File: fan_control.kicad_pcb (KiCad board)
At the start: 2 copper layers, 50 x 68.6 mm, 46 parts, among them J1 Conn_01x02_Male, J2 Conn_01x02_Male, J3 Conn_01x02_Male, J4 Conn_01x02_Male, J5 Conn_01x02_Male, J6 Conn_01x02_Male, J7 Conn_01x02_Male, J8 Conn_01x02_Male, Q10 BC557, Q11 BC557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

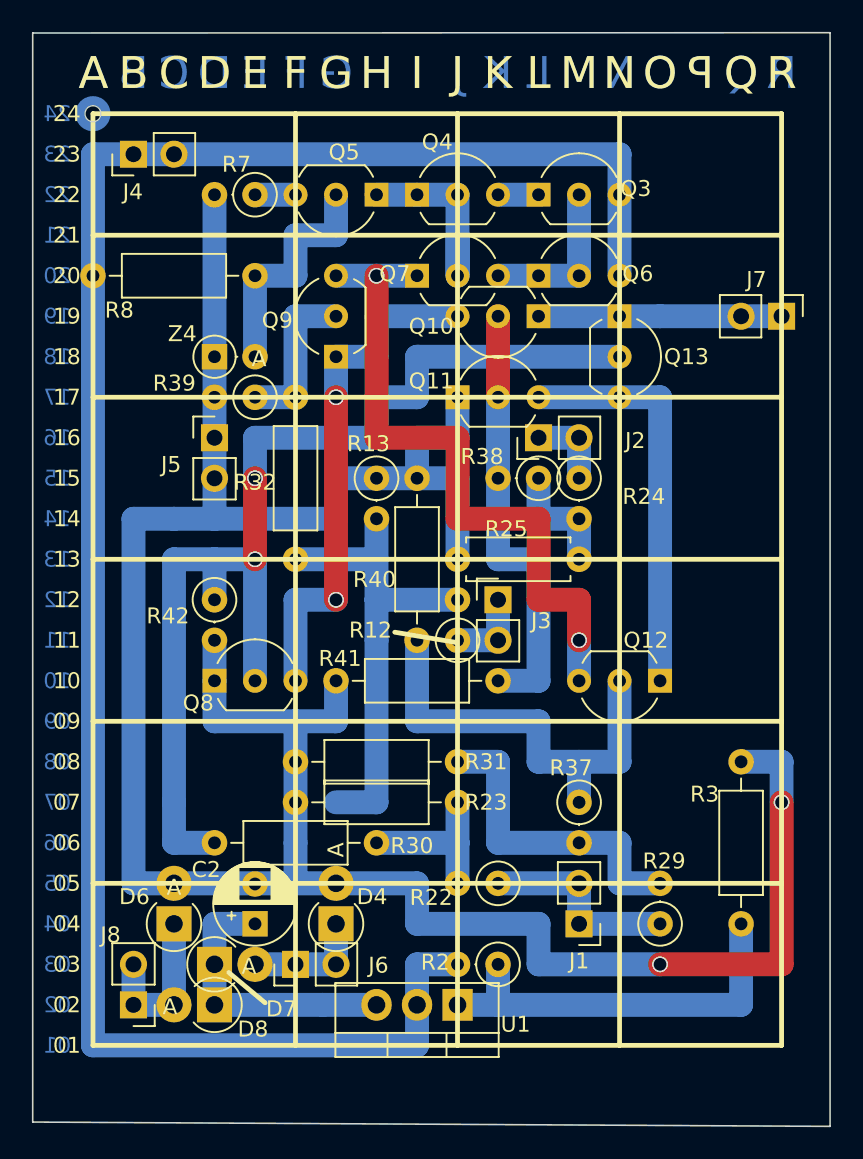
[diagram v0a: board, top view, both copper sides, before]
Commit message: add resistors to pcb
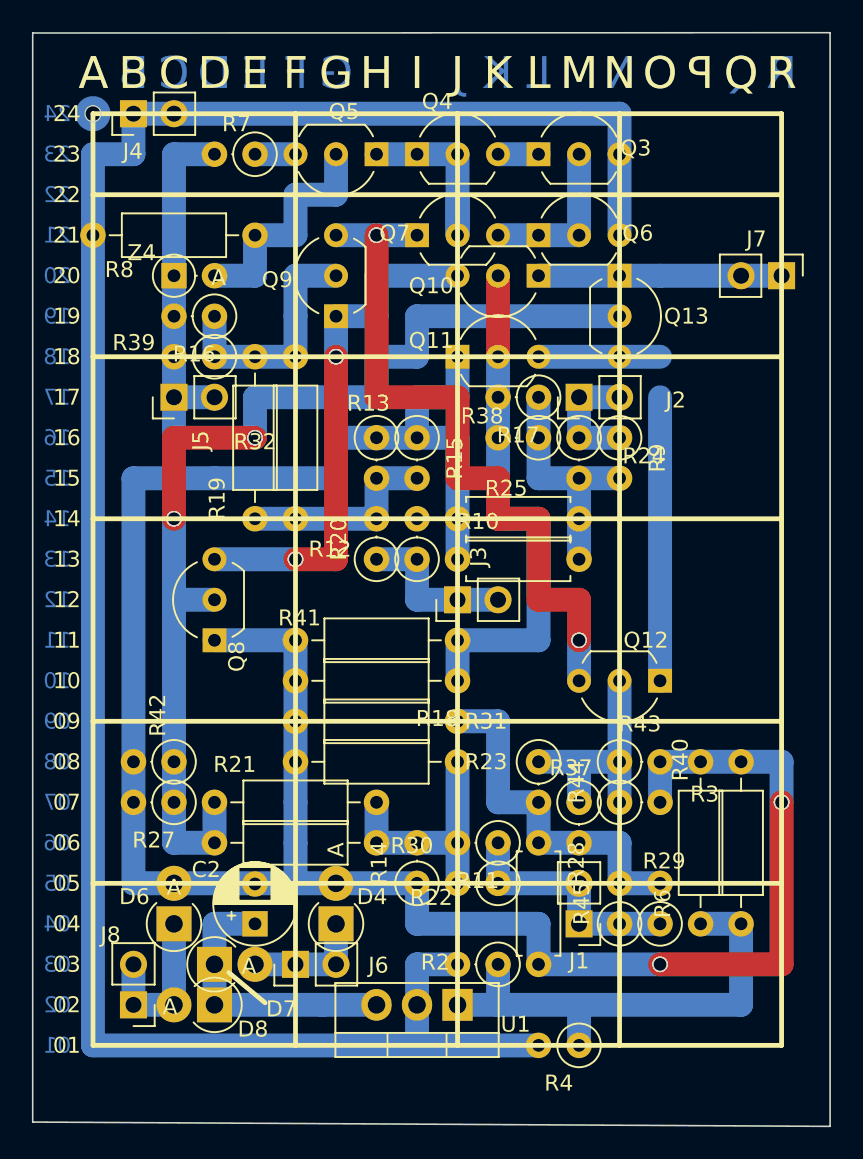
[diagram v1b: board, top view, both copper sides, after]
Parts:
- added R10: 100K, Resistor_THT:R_Axial_DIN0207_L6.3mm_D2.5mm_P7.62mm_Horizontal, F.Cu at (67.2, 63.5)
- added R11: 150K, Resistor_THT:R_Axial_DIN0207_L6.3mm_D2.5mm_P2.54mm_Vertical, F.Cu at (69.7, 81.3)
- added R14: 50K, Resistor_THT:R_Axial_DIN0207_L6.3mm_D2.5mm_P2.54mm_Vertical, F.Cu at (64.7, 83.9)
- added R15: 50k, Resistor_THT:R_Axial_DIN0207_L6.3mm_D2.5mm_P2.54mm_Vertical, F.Cu at (64.7, 55.9)
- added R16: 100K, Resistor_THT:R_Axial_DIN0207_L6.3mm_D2.5mm_P2.54mm_Vertical, F.Cu at (52.0, 48.3)
- added R17: 100K, Resistor_THT:R_Axial_DIN0207_L6.3mm_D2.5mm_P2.54mm_Vertical, F.Cu at (72.3, 53.4)
- added R18: 100K, Resistor_THT:R_Axial_DIN0207_L6.3mm_D2.5mm_P10.16mm_Horizontal, F.Cu at (67.2, 71.2)
- added R19: 100K, Resistor_THT:R_Axial_DIN0207_L6.3mm_D2.5mm_P10.16mm_Horizontal, F.Cu at (54.5, 61.0)
- added R20: 150k, Resistor_THT:R_Axial_DIN0207_L6.3mm_D2.5mm_P2.54mm_Vertical, F.Cu at (62.1, 63.5)
- added R21: 100K, Resistor_THT:R_Axial_DIN0207_L6.3mm_D2.5mm_P10.16mm_Horizontal, F.Cu at (52.0, 78.8)
- added R27: 100K, Resistor_THT:R_Axial_DIN0207_L6.3mm_D2.5mm_P2.54mm_Vertical, F.Cu at (49.4, 78.8)
- added R28: 50K, Resistor_THT:R_Axial_DIN0207_L6.3mm_D2.5mm_P7.62mm_Horizontal, F.Cu at (72.3, 81.3)
- added R4: R, Resistor_THT:R_Axial_DIN0207_L6.3mm_D2.5mm_P2.54mm_Vertical, F.Cu at (74.8, 94.0)
- added R43: 100K, Resistor_THT:R_Axial_DIN0207_L6.3mm_D2.5mm_P2.54mm_Vertical, F.Cu at (77.4, 76.2)
- added R44: 100K, Resistor_THT:R_Axial_DIN0207_L6.3mm_D2.5mm_P2.54mm_Vertical, F.Cu at (72.3, 76.2)
- added R45: 150K, Resistor_THT:R_Axial_DIN0207_L6.3mm_D2.5mm_P2.54mm_Vertical, F.Cu at (77.4, 86.4)
- added R6: R, Resistor_THT:R_Axial_DIN0207_L6.3mm_D2.5mm_P10.16mm_Horizontal, F.Cu at (82.4, 86.4)
- added R9: 300K, Resistor_THT:R_Axial_DIN0207_L6.3mm_D2.5mm_P2.54mm_Vertical, F.Cu at (77.4, 55.9)
- R40: footprint Resistor_THT:R_Axial_DIN0207_L6.3mm_D2.5mm_P10.16mm_Horizontal -> Resistor_THT:R_Axial_DIN0207_L6.3mm_D2.5mm_P2.54mm_Vertical
- moved R40 16.3 mm to (77.4, 78.8), turned to 0 degrees
- moved R42 10.5 mm to (49.4, 76.2), turned to 180 degrees
- moved Z4 5.68 mm to (49.4, 45.8)
- moved R12 5.68 mm to (64.7, 63.5)
- moved R41 3.59 mm to (67.2, 68.6)
- moved J2 3.59 mm to (74.8, 53.4)
- moved J5 3.59 mm to (49.4, 53.4), turned to 90 degrees
- moved R39 3.59 mm to (52.0, 50.8)
- moved J3 2.54 mm to (67.2, 66.1), turned to 90 degrees
- moved Q8 2.54 mm to (52.0, 68.6), turned to 90 degrees
- moved Q9 2.54 mm to (59.6, 48.3)
- moved R31 2.54 mm to (67.2, 73.7)
- moved J4 2.54 mm to (46.9, 35.6)
- moved J7 2.54 mm to (87.5, 45.8)
- moved Q10 2.54 mm to (72.3, 45.8)
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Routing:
- net Net-(R12-Pad2): track 30.5 -> 12.7 mm
- net 0: track 165.1 -> 177.8 mm
- net bias_r: track 27.9 -> 15.2 mm
- net +15V: track 124.5 -> 134.6 mm
- net Net-(R10-Pad2): track 7.62 -> 15.2 mm
- net C: track 5.08 -> 10.2 mm
- net bias_l: track 10.2 -> 15.2 mm
- net bias_i: track 27.9 -> 33.0 mm
- net Net-(R2-Pad1): track 25.4 -> 30.5 mm
- net Net-(R11-Pad2): track 10.2 -> 15.2 mm
- net bias_o: track 71.1 -> 68.6 mm
- net Net-(R28-Pad1): track 20.3 -> 22.9 mm
- net E: track 12.7 -> 15.2 mm
- net B: track 5.08 -> 7.62 mm
- net Net-(Q12-Pad3): track 43.2 -> 45.7 mm

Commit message: add silkscreen references
...
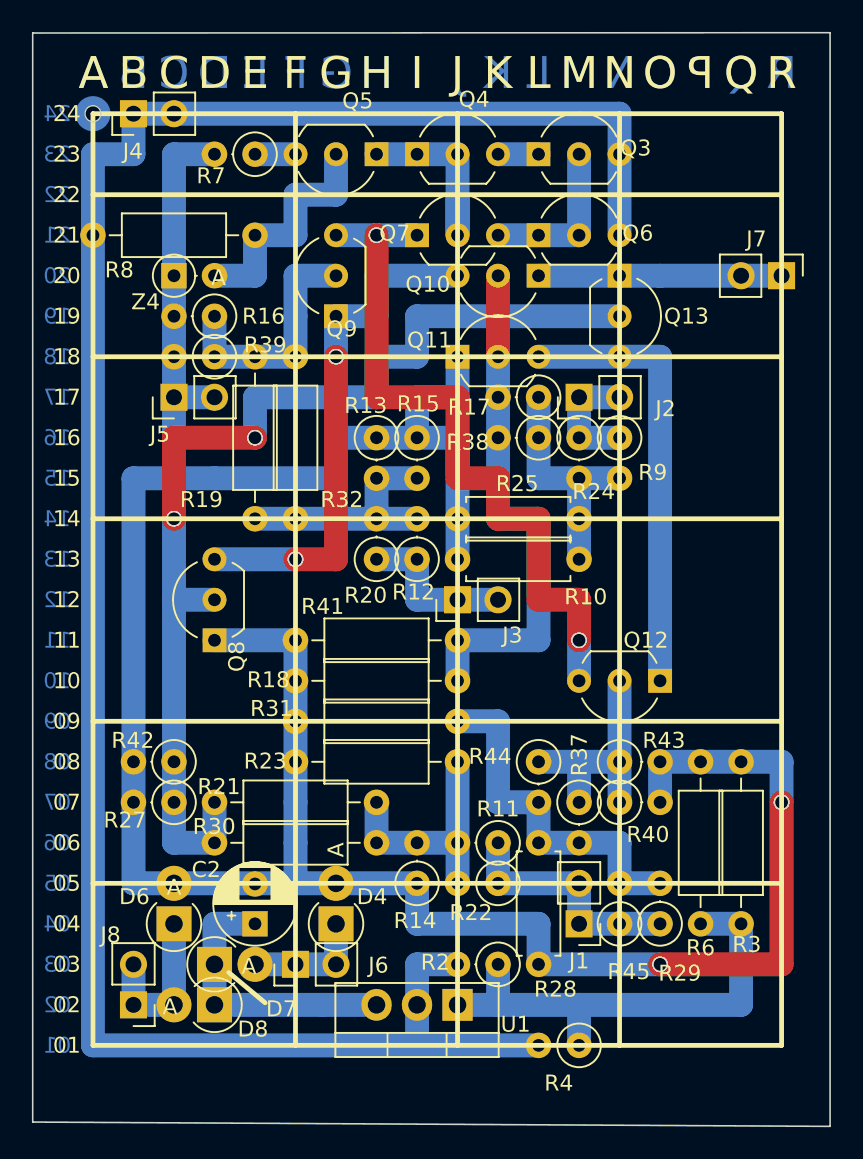
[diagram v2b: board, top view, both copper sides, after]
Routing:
- net Net-(R12-Pad2): track 12.7 -> 15.2 mm
- net Net-(Q11-Pad3): track 25.4 -> 27.9 mm
